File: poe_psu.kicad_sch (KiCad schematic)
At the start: 48 parts, among them T1 HR051142, U2 SI3404-A-GM, U3 EL3H7-G, U4 AN431

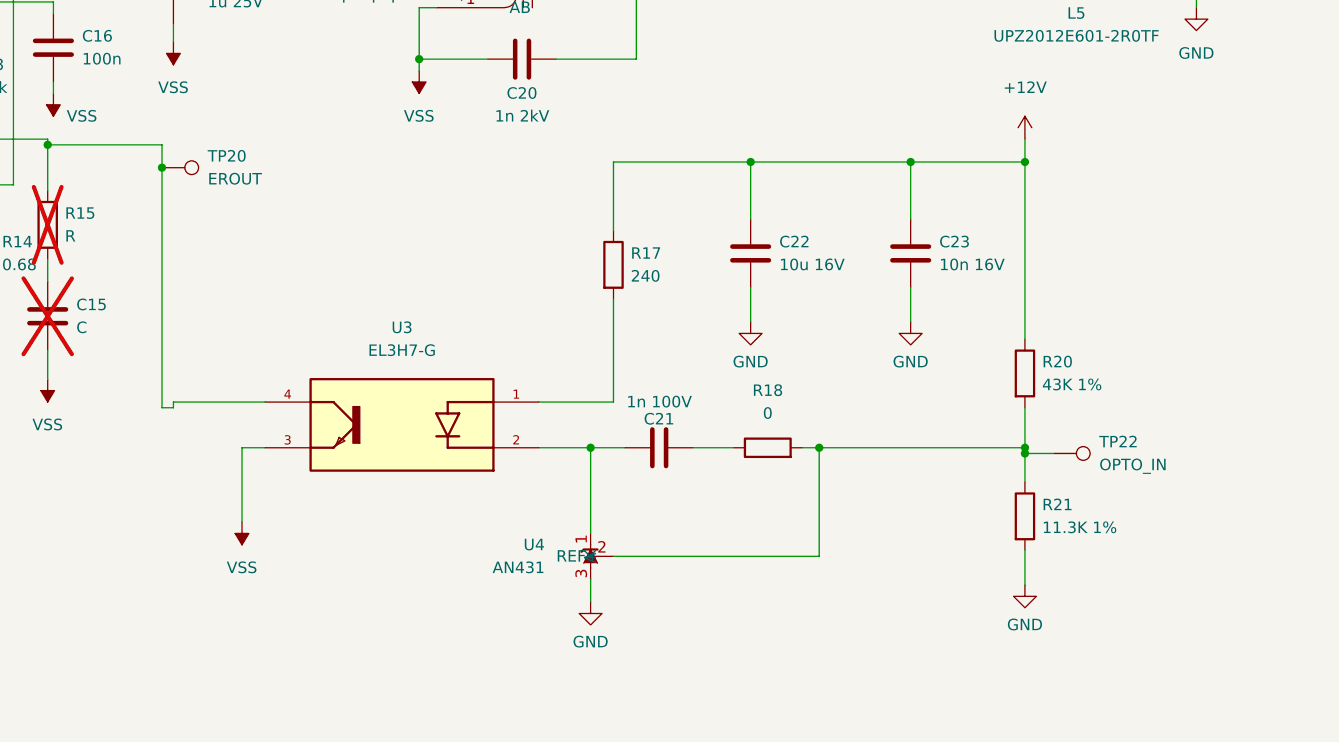
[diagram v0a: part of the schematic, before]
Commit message: Remove custom library for EL3H7, use the kicad one.
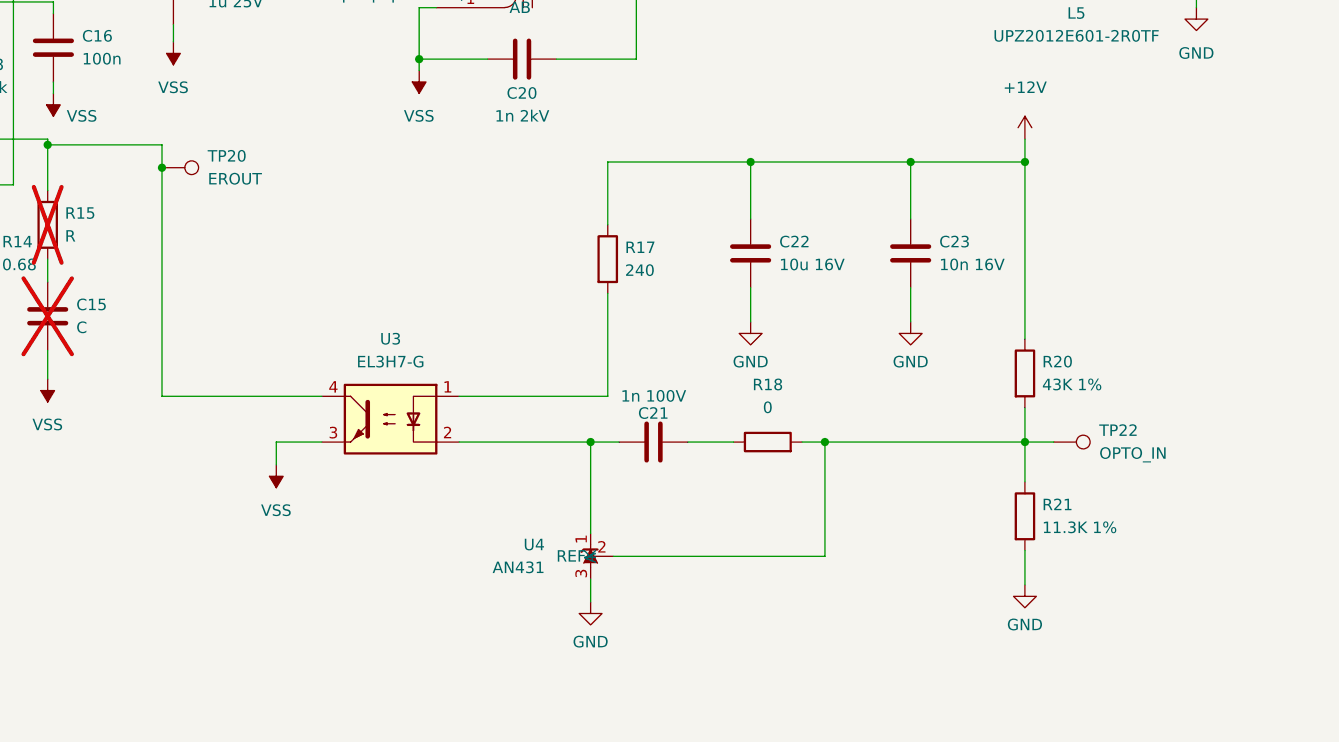
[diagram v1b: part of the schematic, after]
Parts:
- removed U3: EL3H7-G, project_footprints:SOIC127P700X200-4N, symbol EL3H7-G:EL3H7-G
- added U3: EL3H7-G, Package_SO:SSOP-4_4.4x2.6mm_P1.27mm, symbol Isolator:Optocoupler_DC_PhotoNPN_AKEC
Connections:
- net VSS: now also U3.3
- net at R17.2: now also U3.1
- net at C21.1, U4.1 (K): now also U3.2
- net at R13.2, R15.1, TP20.1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: now also U3.4
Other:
- moved on the sheet: C21, R17, R18, TP22

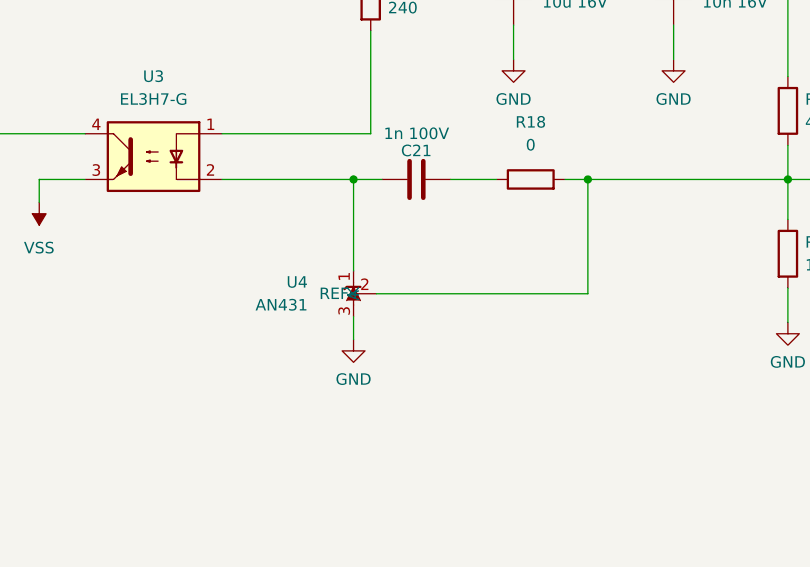
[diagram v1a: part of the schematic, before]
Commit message: Use kicad built-in symbol for AN431.
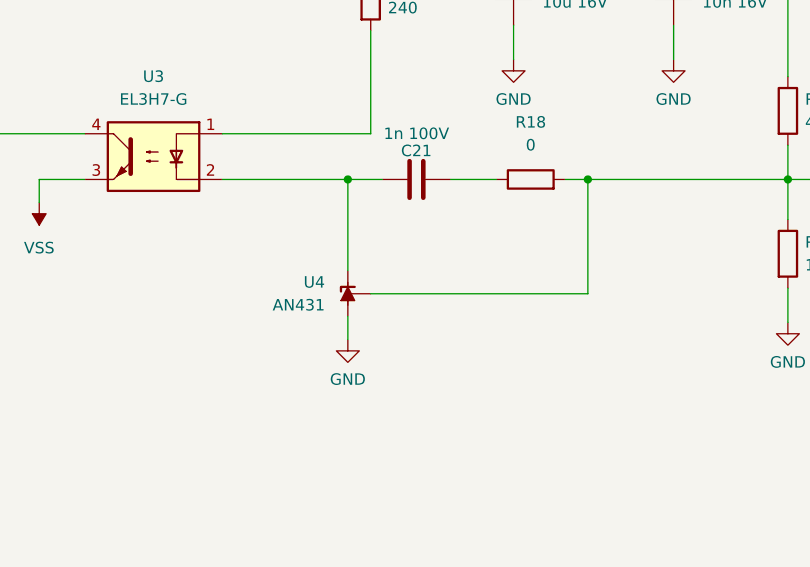
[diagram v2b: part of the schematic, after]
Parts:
- removed U4: AN431, Package_TO_SOT_SMD:SOT-23, symbol AN431:AN431
- added U4: AN431, Package_TO_SOT_SMD:SOT-23, symbol Reference_Voltage:TL431DBZ
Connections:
- net GND: now also U4.3 (A)
- net at C21.1, U3.2: now also U4.1 (K)
- net at R18.2, R20.2, R21.1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: now also U4.2 (REF)
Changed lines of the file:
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@@
 	)
 	(junction
-		(at 208.915 129.54)
+		(at 208.28 129.54)
 		(diameter 0)
 		(color 0 0 0 0)
@@
 	(wire
 		(pts
-			(xy 161.29 99.06) (xy 161.29 124.46)
+			(xy 208.28 129.54) (xy 212.09 129.54)
 		)
 		(stroke
@@
 	(wire
 		(pts
-			(xy 161.29 99.06) (xy 161.29 96.52)
+			(xy 161.29 99.06) (xy 161.29 124.46)
 		)
 		(stroke
@@
 	(wire
 		(pts
-			(xy 133.35 103.505) (xy 140.97 103.505)
+			(xy 161.29 99.06) (xy 161.29 96.52)
 		)
 		(stroke
@@
 	(wire
 		(pts
-			(xy 140.97 112.395) (xy 140.97 116.205)
+			(xy 133.35 103.505) (xy 140.97 103.505)
 		)
 		(stroke
@@
 	(wire
 		(pts
-			(xy 136.525 116.205) (xy 136.525 111.125)
+			(xy 140.97 112.395) (xy 140.97 116.205)
 		)
 		(stroke
@@
 	(wire
 		(pts
-			(xy 74.93 93.345) (xy 90.17 93.345)
+			(xy 136.525 116.205) (xy 136.525 111.125)
 		)
 		(stroke
@@
 	(wire
 		(pts
-			(xy 213.995 52.07) (xy 219.71 52.07)
+			(xy 74.93 93.345) (xy 90.17 93.345)
 		)
 		(stroke
@@
 	(wire
 		(pts
-			(xy 211.455 142.24) (xy 234.95 142.24)
+			(xy 213.995 52.07) (xy 219.71 52.07)
 		)
 		(stroke
@@
 	(wire
 		(pts
+			(xy 210.82 142.24) (xy 234.95 142.24)
+		)
+		(stroke
+			(width 0)
+			(type default)
+		)
+	)
+	(wire
+		(pts
 			(xy 133.35 103.505) (xy 130.81 103.505)
 		)
@@
 	(wire
 		(pts
-			(xy 194.31 129.54) (xy 208.915 129.54)
+			(xy 194.31 129.54) (xy 208.28 129.54)
 		)
 		(stroke
@@
 	(wire
 		(pts
-			(xy 208.915 129.54) (xy 212.09 129.54)
-		)
-		(stroke
-			(width 0)
-			(type default)
-		)
-	)
-	(wire
-		(pts
 			(xy 160.02 73.66) (xy 162.56 73.66)
 		)
@@
 	(wire
 		(pts
-			(xy 208.915 144.78) (xy 208.915 147.32)
+			(xy 208.28 144.78) (xy 208.28 147.32)
 		)
 		(stroke
@@
 	(wire
 		(pts
-			(xy 208.915 139.7) (xy 208.915 129.54)
+			(xy 208.28 139.7) (xy 208.28 129.54)
 		)
 		(stroke
@@
 	(symbol
 		(lib_id "power:GND")
-		(at 208.915 147.32 0)
+		(at 208.28 147.32 0)
 		(unit 1)
 		(exclude_from_sim no)
@@
 		(fields_autoplaced yes)
 		(property "Reference" "#PWR030"
-			(at 208.915 153.67 0)
+			(at 208.28 153.67 0)
 			(effects
 				(font
@@
 		)
 		(property "Value" "GND"
-			(at 208.915 151.765 0)
+			(at 208.28 151.765 0)
 			(effects
 				(font
@@
 		)
 		(property "Footprint" ""
-			(at 208.915 147.32 0)
+			(at 208.28 147.32 0)
 			(effects
 				(font
@@
 		)
 		(property "Datasheet" ""
-			(at 208.915 147.32 0)
+			(at 208.28 147.32 0)
 			(effects
 				(font
@@
 		)
 		(property "Description" ""
-			(at 208.915 147.32 0)
+			(at 208.28 147.32 0)
 			(effects
 				(font
@@
 	)
 	(symbol
+		(lib_id "Reference_Voltage:TL431DBZ")
+		(at 208.28 142.24 270)
+		(mirror x)
+		(unit 1)
+		(exclude_from_sim no)
+		(in_bom yes)
+		(on_board yes)
+		(dnp no)
+		(property "Reference" "U4"
+			(at 205.74 140.9699 90)
+			(effects
+				(font
+					(size 1.27 1.27)
+				)
+				(justify right)
+			)
+		)
+		(property "Value" "AN431"
+			(at 205.74 143.5099 90)
+			(effects
+				(font
+					(size 1.27 1.27)
+				)
+				(justify right)
+			)
+		)
+		(property "Footprint" "Package_TO_SOT_SMD:SOT-23"
+			(at 203.454 142.24 0)
+			(effects
+				(font
+					(size 1.27 1.27)
+					(italic yes)
+				)
+				(hide yes)
+			)
+		)
+		(property "Datasheet" "https://www.diodes.com/assets/Datasheets/AN431.pdf"
+			(at 199.136 140.462 0)
+			(effects
+				(font
+					(size 1.27 1.27)
+					(italic yes)
+				)
+				(hide yes)
+			)
+		)
+		(property "Description" "Shunt Regulator, SOT-23"
+			(at 201.168 142.24 0)
+			(effects
+				(font
+					(size 1.27 1.27)
+				)
+				(hide yes)
+			)
+		)
+		(property "LCSC" "C97717"
+			(at 208.28 142.24 90)
+			(effects
+				(font
+					(size 1.27 1.27)
+				)
+				(hide yes)
+			)
+		)
+		(pin "3"
+		)
+		(pin "2"
+		)
+		(pin "1"
+		)
+		(instances
+			(project ""
+				(path "/727d6c0a-a0ef-4feb-9656-3db3cb90564a/0dd39886-6ed0-43ed-af54-4a02cc0bde41"
+					(reference "U4")
+					(unit 1)
+				)
+			)
+		)
+	)
+	(symbol
 		(lib_id "power:GND")
 		(at 226.695 116.205 0)
@@
 					(unit 1)
 				)
-			)
-		)
-	)
-	(symbol
-		(lib_id "AN431:AN431")
-		(at 208.915 142.24 270)
-		(mirror x)
-		(unit 1)
-		(exclude_from_sim no)
-		(in_bom yes)
-		(on_board yes)
-		(dnp no)
-		(property "Reference" "U4"
-			(at 203.835 140.97 90)
-			(effects
-				(font
-					(size 1.27 1.27)
-				)
-				(justify right)
-			)
-		)
-		(property "Value" "AN431"
-			(at 203.835 143.51 90)
-			(effects
-				(font
-					(size 1.27 1.27)
-				)
-				(justify right)
-			)
-		)
-		(property "Footprint" "Package_TO_SOT_SMD:SOT-23"
-			(at 208.915 142.24 0)
-			(effects
-				(font
-					(size 1.27 1.27)
-				)
-				(hide yes)
-			)
-		)
-		(property "Datasheet" ""
-			(at 208.915 142.24 0)
-			(effects
-				(font
-					(size 1.27 1.27)
-				)
-				(hide yes)
-			)
-		)
-		(property "Description" ""
-			(at 208.915 142.24 0)
-			(effects
-				(font
-					(size 1.27 1.27)
-				)
-				(hide yes)
-			)
-		)
-		(property "LCSC" "C97717"
-			(at 208.915 142.24 90)
-			(effects
-				(font
-					(size 1.27 1.27)
-				)
-				(hide yes)
-			)
-		)
-		(pin "1"
-		)
-		(pin "2"
-		)
-		(pin "3"
-		)
-		(instances
-			(project ""
-				(path "/727d6c0a-a0ef-4feb-9656-3db3cb90564a/0dd39886-6ed0-43ed-af54-4a02cc0bde41"
-					(reference "U4")
-					(unit 1)
-				)

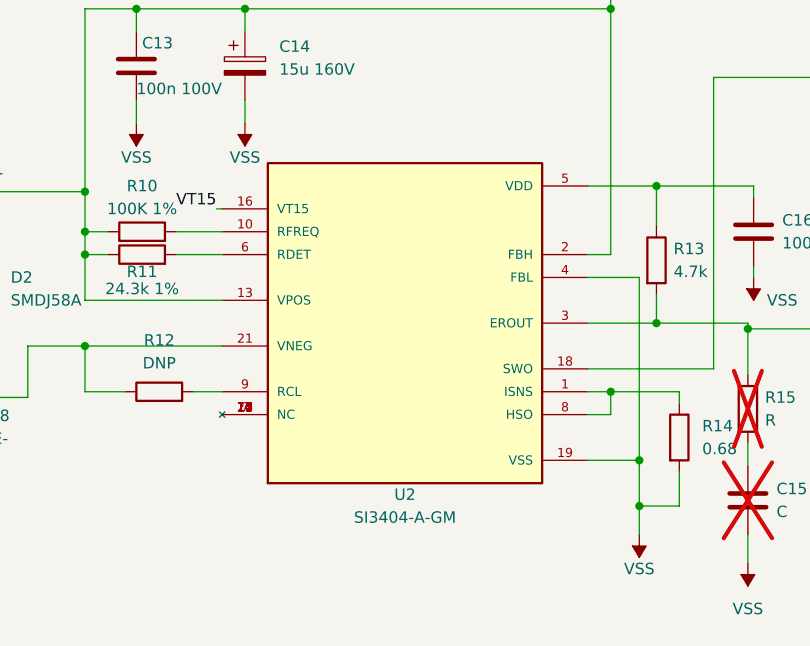
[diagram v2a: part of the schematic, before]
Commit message: remove custom footprint for Si3404
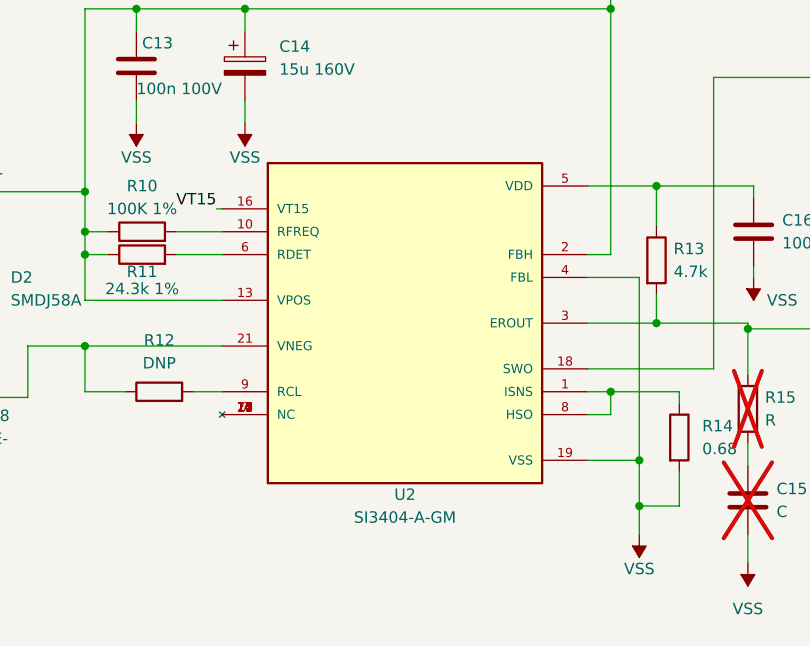
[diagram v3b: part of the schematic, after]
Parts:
- U2: footprint project_footprints:QFN50P400X400X90-21N -> Package_DFN_QFN:MLF-20-1EP_4x4mm_P0.5mm_EP2.6x2.6mm_ThermalVias
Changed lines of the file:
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@@
 			)
 		)
-		(property "Footprint" "project_footprints:QFN50P400X400X90-21N"
+		(property "Footprint" "Package_DFN_QFN:MLF-20-1EP_4x4mm_P0.5mm_EP2.6x2.6mm_ThermalVias"
 			(at 110.49 95.885 0)
 			(effects

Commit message: Finish preliminary routing
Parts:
- removed TP17: POE+, TestPoint:TestPoint_Pad_D1.5mm, symbol Connector:TestPoint
- removed TP18: POE-, TestPoint:TestPoint_Pad_D1.5mm, symbol Connector:TestPoint
- removed TP21: FBH, TestPoint:TestPoint_Pad_D1.5mm, symbol Connector:TestPoint
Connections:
- net POE+_OUT: now reaches C12.1, C13.1, C14.1, C18.1, C19.1, D2.1 (K), L2.2, R10.1, R11.1, R16.1, T1.4 (PB), U2.13 (VPOS), U2.2 (FBH)
- net POE-_OUT: now reaches C12.2, D2.2 (A), L3.2, R12.1, U2.21 (VNEG)

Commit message: BOM updates
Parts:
- L3: LCSC (none) -> C356979
- R12: now not fitted
- R16: LCSC (none) -> C2906991
- R17: LCSC C5140966 -> C2907130
- R18: LCSC (none) -> C100044
- TP19, TP20, TP22, TP23: now left out of the parts list

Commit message: Zamkonator rev 1.3
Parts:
- renumbered C11 to C13, C12 to C14, C13 to C15, C14 to C16, C15 to C17, C16 to C18, C17 to C19, C18 to C20, C19 to C21, C20 to C22, C21 to C23, C22 to C24, C24 to C25, C25 to C26, C23 to C27, C26 to C28, D5 to D10, D6 to D11, D2 to D7, D3 to D8, D4 to D9, R10 to R17, R11 to R18, R12 to R19, R13 to R20, R14 to R21, R15 to R22, R16 to R23, R17 to R24, R19 to R25, R18 to R26, R20 to R27, R21 to R28, TP23 to TP17, TP19 to TP18, TP20 to TP19, TP22 to TP20, U2 to U3, U3 to U4, U4 to U5

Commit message: Rev 1.3, BOM optimizations
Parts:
- C18: value 100n -> 100n 100V
- C26: value 100n 16V -> 100n 100V
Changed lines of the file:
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@@
 			)
 		)
-		(property "Value" "100n"
+		(property "Value" "100n 100V"
 			(at 152.4 86.9949 0)
 			(show_name no)
@@
 			)
 		)
-		(property "Value" "100n 16V"
+		(property "Value" "100n 100V"
 			(at 241.3 71.7549 0)
 			(show_name no)
